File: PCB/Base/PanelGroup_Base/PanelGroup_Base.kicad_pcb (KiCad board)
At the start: 2 copper layers, 98 x 78.5 mm, 63 parts, among them J1 J_DIAG, J11 J_BREAKOUT, J2 J_BL1, J3 J_I2C2, J4 J_I2C1, J5 J_CAN_TERM, J6 J_BL2, J7 J_SWD, J8 J_BUS_IN, J9 J_BUS_OUT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

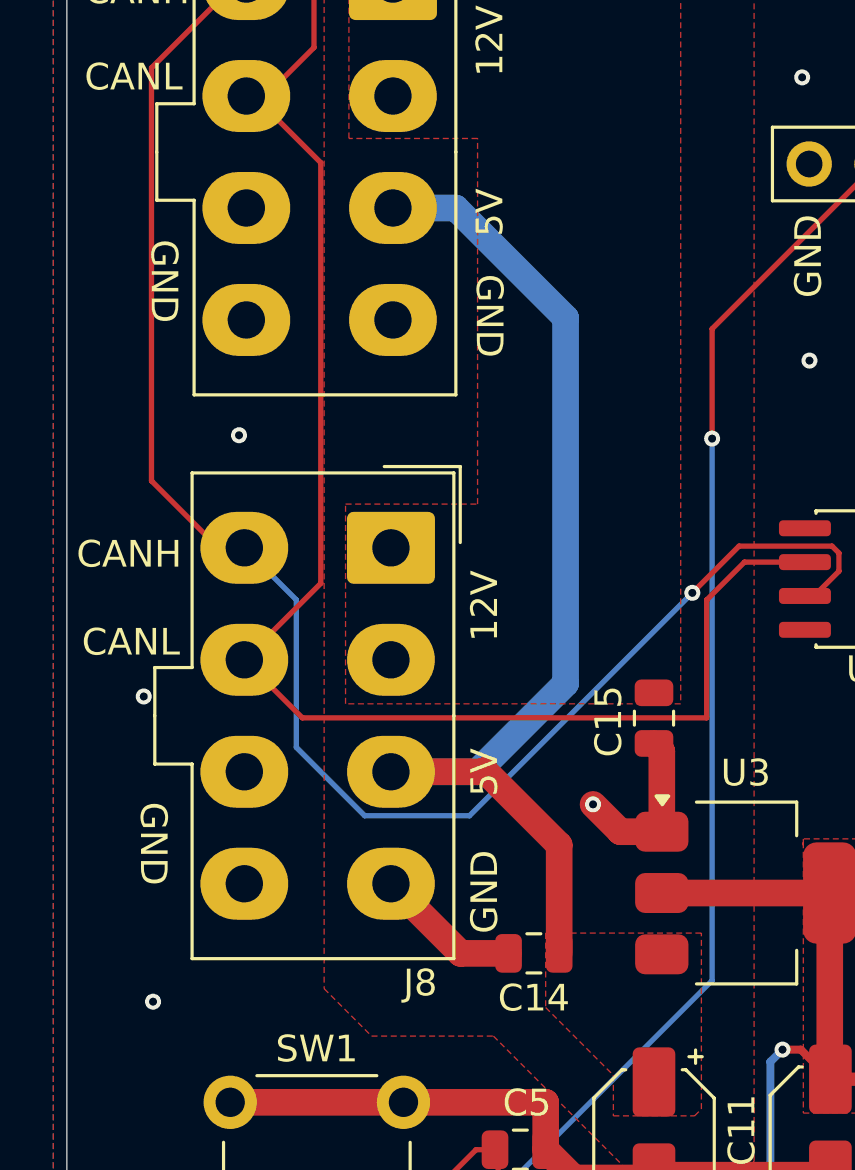
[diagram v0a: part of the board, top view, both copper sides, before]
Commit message: feat(pcb): bus power distribution — poured rails, solid bus pads, GND stitching (base boards)
PanelGroup_Base + Gateway/Bridge: +12V/+5V/GND poured (12V top, 5V bottom,
GND both layers), solid pad connection on J_BUS power+GND pins (CAN default),
GND stitching vias. Sized for per-console injection (5A/12V, 2A/5V); copper
poured so the connector (8-9A/pin) is the limit, not traces.
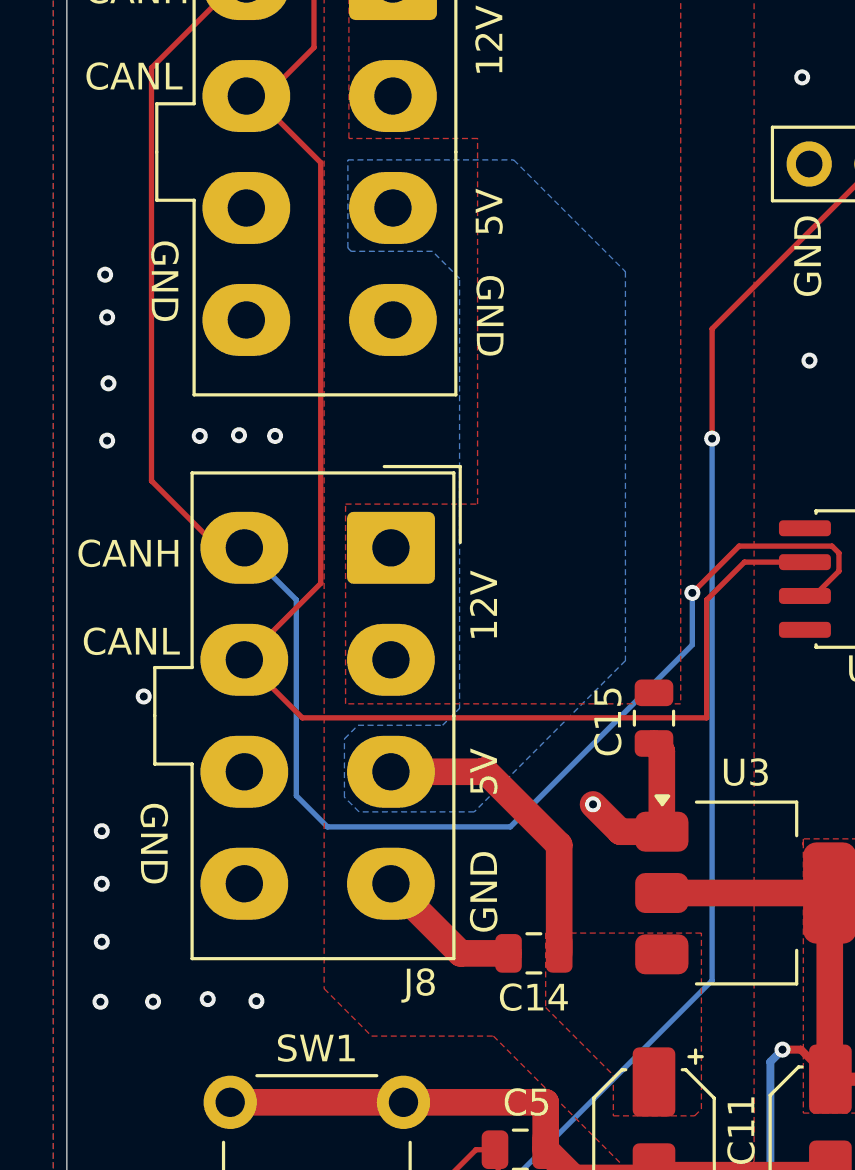
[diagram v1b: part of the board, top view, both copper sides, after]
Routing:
- net +5V: track 41.4 -> 11.6 mm
- net /CANH: track 78.6 -> 81.1 mm
- net GND: vias 67 -> 79
- added copper zone on B.Cu, net +5V
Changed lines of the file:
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@@
 			(pinfunction "Pin_3_3")
 			(pintype "passive")
+			(zone_connect 2)
 		)
 		(pad "4" thru_hole oval
@@
 			(pinfunction "Pin_4_4")
 			(pintype "passive")
+			(zone_connect 2)
 		)
 		(pad "5" thru_hole oval
@@
 			(pinfunction "Pin_7_7")
 			(pintype "passive")
+			(zone_connect 2)
 		)
 		(pad "8" thru_hole oval
@@
 			(pinfunction "Pin_8_8")
 			(pintype "passive")
+			(zone_connect 2)
 		)
 		(embedded_fonts no)
@@
 		(tags "connector Molex Mini-Fit_Jr vertical")
 		(property "Reference" "J9"
-			(at -3.925 -1.926 180)
+			(at -3.925 -1.926 0)
 			(layer "F.SilkS")
 			(effects
@@
 			(pinfunction "Pin_3_3")
 			(pintype "passive")
+			(zone_connect 2)
 		)
 		(pad "4" thru_hole oval
@@
 			(pinfunction "Pin_4_4")
 			(pintype "passive")
+			(zone_connect 2)
 		)
 		(pad "5" thru_hole oval
@@
 			(pinfunction "Pin_7_7")
 			(pintype "passive")
+			(zone_connect 2)
 		)
 		(pad "8" thru_hole oval
@@
 			(pinfunction "Pin_8_8")
 			(pintype "passive")
+			(zone_connect 2)
 		)
 		(embedded_fonts no)
@@
 	)
 	(segment
-		(start 117.590918 111.5976)
-		(end 113.663548 111.5976)
+		(start 111.097 110.843)
+		(end 111.097 103.4976)
 		(width 0.2)
 		(layer "B.Cu")
@@
 	)
 	(segment
-		(start 111.097 109.031052)
-		(end 111.097 103.4976)
+		(start 119.126 112.014)
+		(end 112.268 112.014)
 		(width 0.2)
 		(layer "B.Cu")
@@
 	)
 	(segment
-		(start 113.663548 111.5976)
-		(end 111.097 109.031052)
+		(start 125.95276 103.235758)
+		(end 125.95276 105.18724)
 		(width 0.2)
 		(layer "B.Cu")
@@
 	)
 	(segment
-		(start 125.95276 103.235758)
-		(end 117.590918 111.5976)
+		(start 112.268 112.014)
+		(end 111.097 110.843)
+		(width 0.2)
+		(layer "B.Cu")
+		(net "/CANH")
+	)
+	(segment
+		(start 125.95276 105.18724)
+		(end 119.126 112.014)
 		(width 0.2)
 		(layer "B.Cu")
@@
 	)
 	(via
+		(at 103.8 116.325)
+		(size 0.6)
+		(drill 0.3)
+		(layers "F.Cu" "B.Cu")
+		(free yes)
+		(net "GND")
+	)
+	(via
+		(at 103.925 91.3)
+		(size 0.6)
+		(drill 0.3)
+		(layers "F.Cu" "B.Cu")
+		(free yes)
+		(net "GND")
+	)
+	(via
 		(at 108.948 97.3226)
 		(size 0.6)
@@
 	)
 	(via
+		(at 107.775 118.475)
+		(size 0.6)
+		(drill 0.3)
+		(layers "F.Cu" "B.Cu")
+		(free yes)
+		(net "GND")
+	)
+	(via
 		(at 199.173 115.6226)
 		(size 0.6)
@@
 	)
 	(via
+		(at 103.8 112.175)
+		(size 0.6)
+		(drill 0.3)
+		(layers "F.Cu" "B.Cu")
+		(free yes)
+		(net "GND")
+	)
+	(via
+		(at 103.8 114.15)
+		(size 0.6)
+		(drill 0.3)
+		(layers "F.Cu" "B.Cu")
+		(free yes)
+		(net "GND")
+	)
+	(via
 		(at 151.923 86.7976)
 		(size 0.6)
@@
 	)
 	(via
+		(at 103.75 118.575)
+		(size 0.6)
+		(drill 0.3)
+		(layers "F.Cu" "B.Cu")
+		(free yes)
+		(net "GND")
+	)
+	(via
+		(at 107.475 97.35)
+		(size 0.6)
+		(drill 0.3)
+		(layers "F.Cu" "B.Cu")
+		(free yes)
+		(net "GND")
+	)
+	(via
 		(at 193.073 69.6476)
 		(size 0.6)
@@
 	)
 	(via
+		(at 104 97.525)
+		(size 0.6)
+		(drill 0.3)
+		(layers "F.Cu" "B.Cu")
+		(free yes)
+		(net "GND")
+	)
+	(via
 		(at 166.073 119.8226)
 		(size 0.6)
@@
 	)
 	(via
+		(at 109.6 118.55)
+		(size 0.6)
+		(drill 0.3)
+		(layers "F.Cu" "B.Cu")
+		(free yes)
+		(net "GND")
+	)
+	(via
 		(at 195.273 100.6476)
 		(size 0.6)
@@
 	)
 	(via
+		(at 104.05 95.375)
+		(size 0.6)
+		(drill 0.3)
+		(layers "F.Cu" "B.Cu")
+		(free yes)
+		(net "GND")
+	)
+	(via
 		(at 142.823 110.9476)
 		(size 0.6)
@@
 	)
 	(via
+		(at 110.3 97.35)
+		(size 0.6)
+		(drill 0.3)
+		(layers "F.Cu" "B.Cu")
+		(free yes)
+		(net "GND")
+	)
+	(via
 		(at 105.373 107.1226)
 		(size 0.6)
@@
 	)
 	(via
+		(at 104 92.9)
+		(size 0.6)
+		(drill 0.3)
+		(layers "F.Cu" "B.Cu")
+		(free yes)
+		(net "GND")
+	)
+	(via
 		(at 111.448 134.5226)
 		(size 0.6)
@@
 	)
 	(segment
-		(start 121.199 106.6366)
-		(end 117.888 109.9476)
-		(width 1)
-		(layer "B.Cu")
-		(net "+5V")
-	)
-	(segment
-		(start 114.722 88.7976)
-		(end 117.076 88.7976)
-		(width 1)
-		(layer "B.Cu")
-		(net "+5V")
-	)
-	(segment
-		(start 117.076 88.7976)
-		(end 121.199 92.9206)
-		(width 1)
-		(layer "B.Cu")
-		(net "+5V")
-	)
-	(segment
-		(start 121.199 92.9206)
-		(end 121.199 106.6366)
-		(width 1)
-		(layer "B.Cu")
-		(net "+5V")
-	)
-	(segment
-		(start 117.888 109.9476)
-		(end 114.647 109.9476)
-		(width 1)
-		(layer "B.Cu")
-		(net "+5V")
-	)
-	(segment
 		(start 109.515 84.5976)
 		(end 109.222 84.5976)
@@
 			)
 		)
+	)
+	(zone
+		(net "+5V")
+		(layer "B.Cu")
+		(name "+5V")
+		(hatch edge 0.5)
+		(priority 5)
+		(connect_pads
+			(clearance 0.25)
+		)
+		(min_thickness 0.25)
+		(fill yes
+			(thermal_gap 0.5)
+			(thermal_bridge_width 0.5)
+			(island_removal_mode 1)
+		)
+		(polygon
+			(pts
+				(xy 113.45 111.45) (xy 112.903 110.903) (xy 112.903 108.712) (xy 113.411 108.204) (xy 116.586 108.204)
+				(xy 117.221 107.569) (xy 117.221 91.44) (xy 116.205 90.424) (xy 113.157 90.424) (xy 113.03 90.297)
+				(xy 113.03 86.995) (xy 119.253 86.995) (xy 123.444 91.186) (xy 123.444 105.781) (xy 117.775 111.45)
+			)
+		)
